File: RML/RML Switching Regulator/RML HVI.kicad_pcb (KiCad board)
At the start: 2 copper layers, 81 x 34 mm, 49 parts, among them J1 Tyco, J2 Tyco, J3 NANOFIT-4PIN, Q1 Q_NMOS_GSD, Q2 Q_NMOS_GSD, U1 TLV3701QDBVREP, U2 HV9961LG-G, U3 Optocoupler, U4 LM555xM, U5 LM1117DT-5.0, U6 74AHC1G02

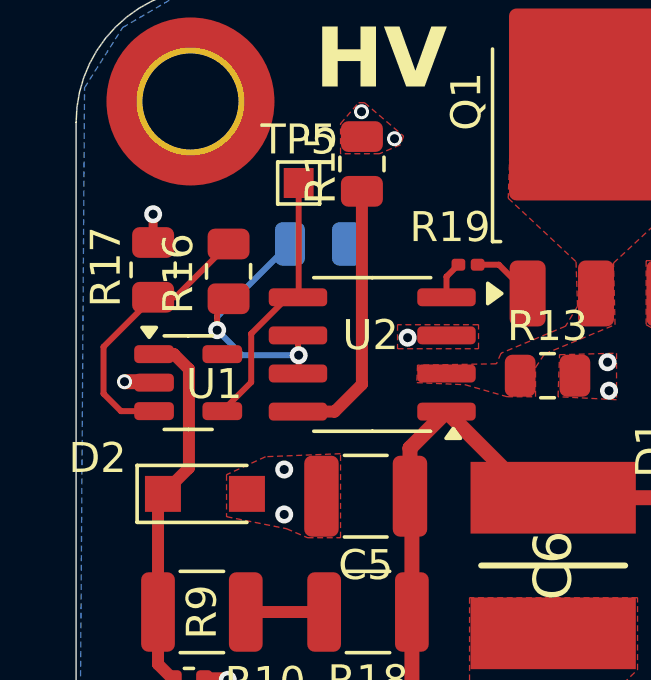
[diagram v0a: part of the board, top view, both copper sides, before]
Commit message: Fixed Small Comparator issue on RML Switiching
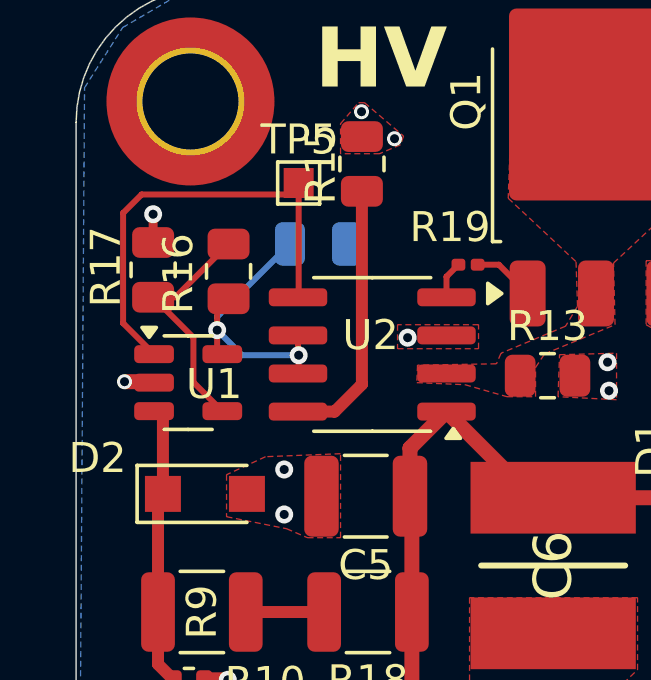
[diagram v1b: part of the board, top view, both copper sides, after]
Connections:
- R16 pad 2: Net-(U1-+) -> Net-(U1--)
- R17 pad 1: Net-(U1-+) -> Net-(U1--)
- U1 pad 1: Net-(D2-K) -> /PWMD
- U1 pad 3: Net-(U1-+) -> Net-(D2-K)
- U1 pad 4: /PWMD -> Net-(U1--)
- U1 pad 5: 7.5V -> +7.5V
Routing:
- net Net-(U1-+): track 9.07 -> 0.00 mm
- net Net-(U1--): track 0.00 -> 8.00 mm
- net /PWMD: track 8.86 -> 15.6 mm
- net Net-(D2-K): track 12.4 -> 9.36 mm
- net +7.5V: track 9.43 -> 10.3 mm
